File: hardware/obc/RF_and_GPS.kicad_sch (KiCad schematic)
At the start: 15 parts, among them J305 SMA RA Connector, J306 SMA RA Connector, J307 SMA RA Connector, U301 BMI088, U302 RFM98PW, U303 S1216V8, U304 GP2S1+

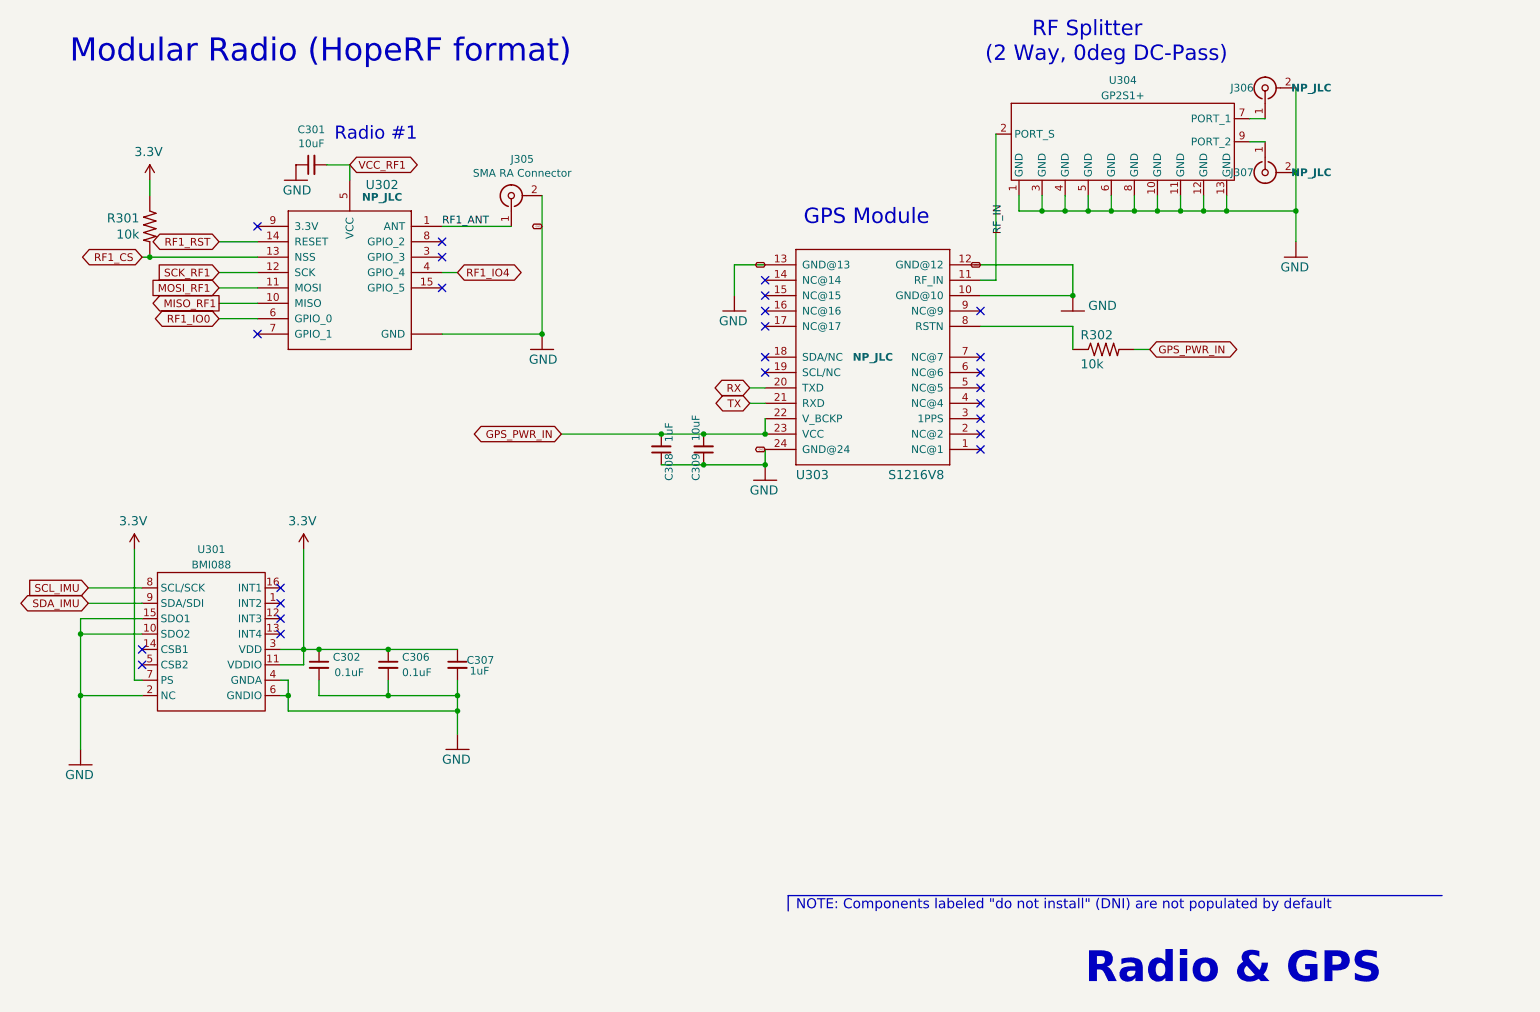
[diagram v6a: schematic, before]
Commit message: obc: Many schematic cleanups
Mostly alignment of components, adjustment of text.

Change SPI resistors to 27 ohms.
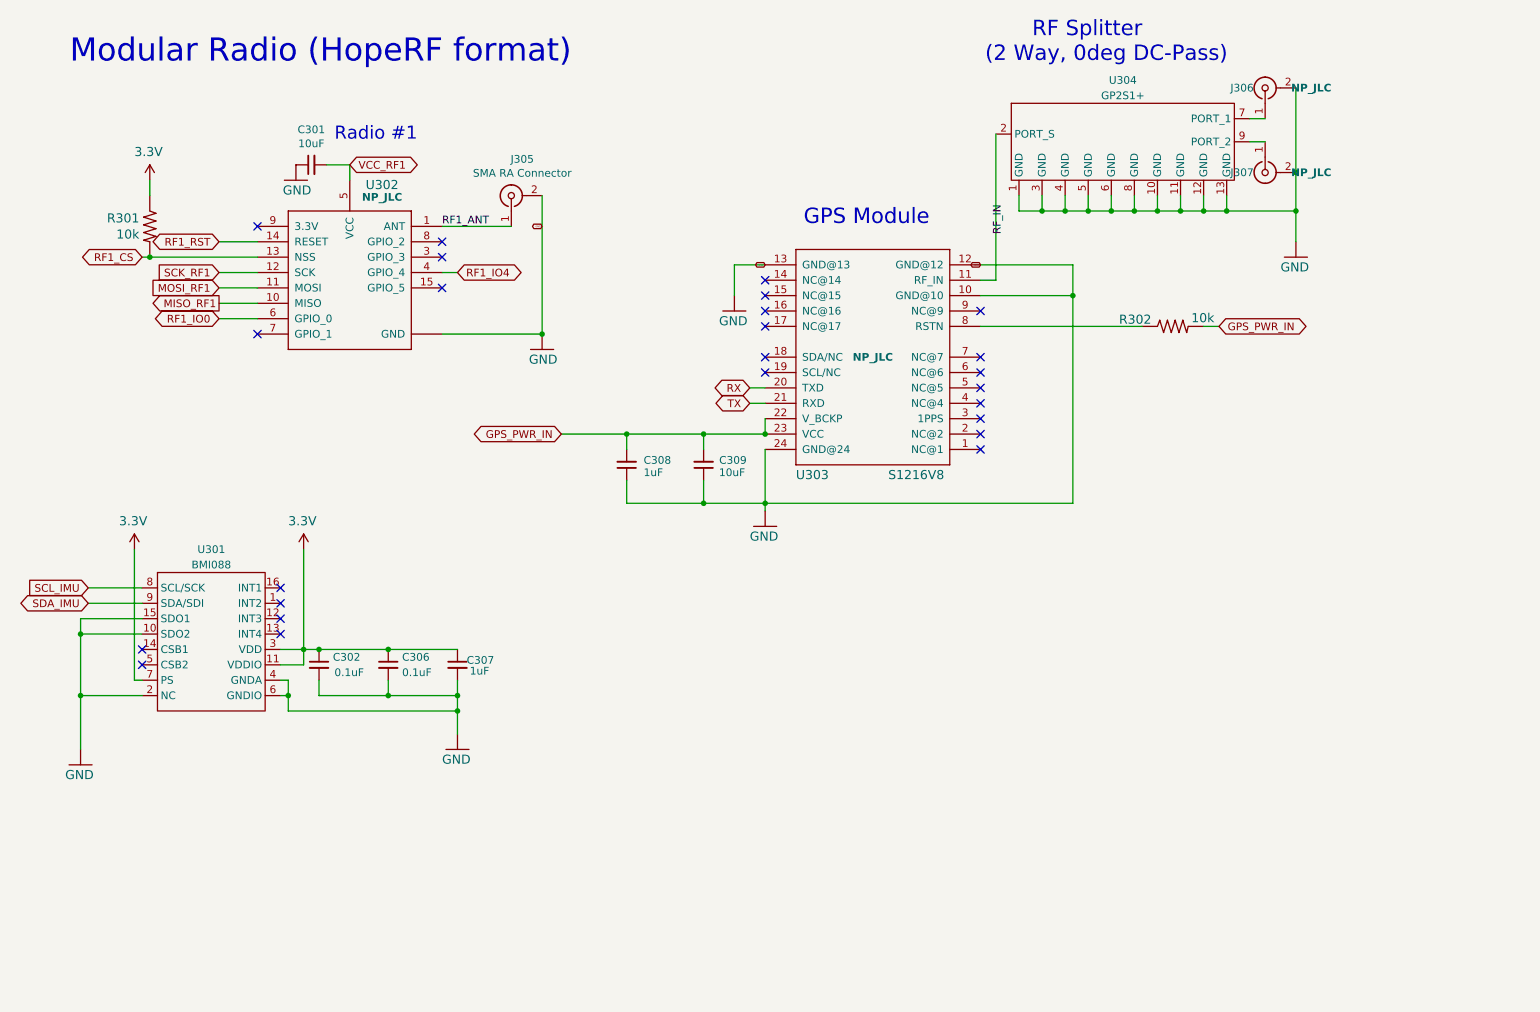
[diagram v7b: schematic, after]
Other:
- note removed: "NOTE: Components labeled "do not install" (DNI) are not populated by default"
- note removed: "Radio & GPS"
- moved on the sheet: C308, C309, R302

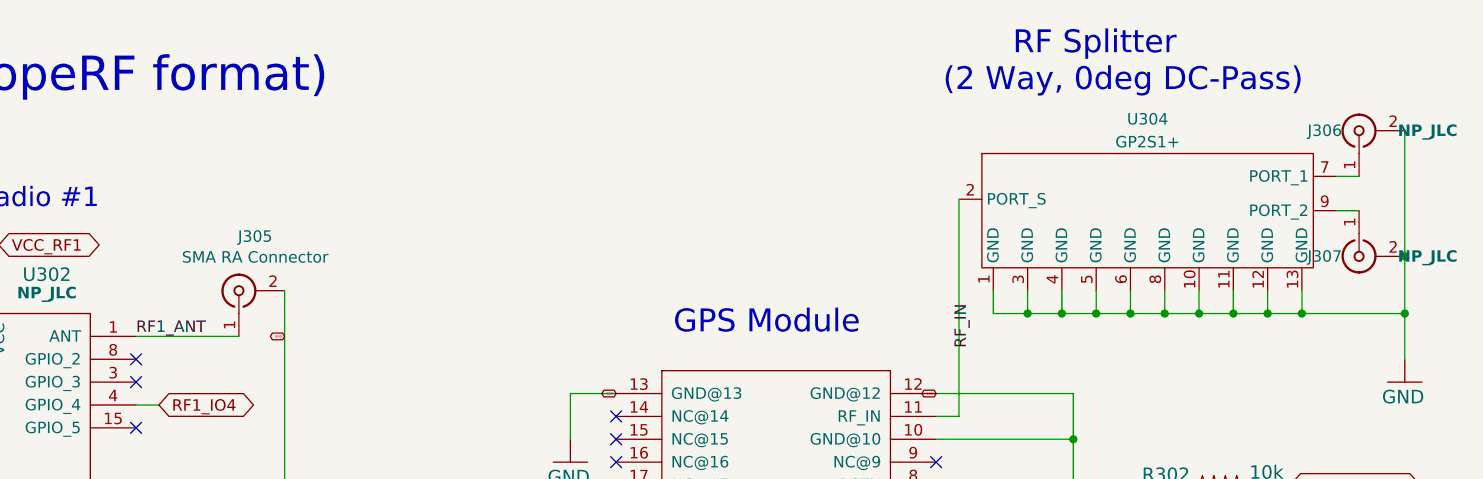
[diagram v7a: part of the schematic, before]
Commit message: obc: final (hopefully) design review for rev B
- Update some text
- Change some part values based on math (greater charge current)
- Increase design conservatism (place pullups on CS)

BOM review still needs to occur, including for a few parts that had
values changed in this pass (without part numbers being chosen)
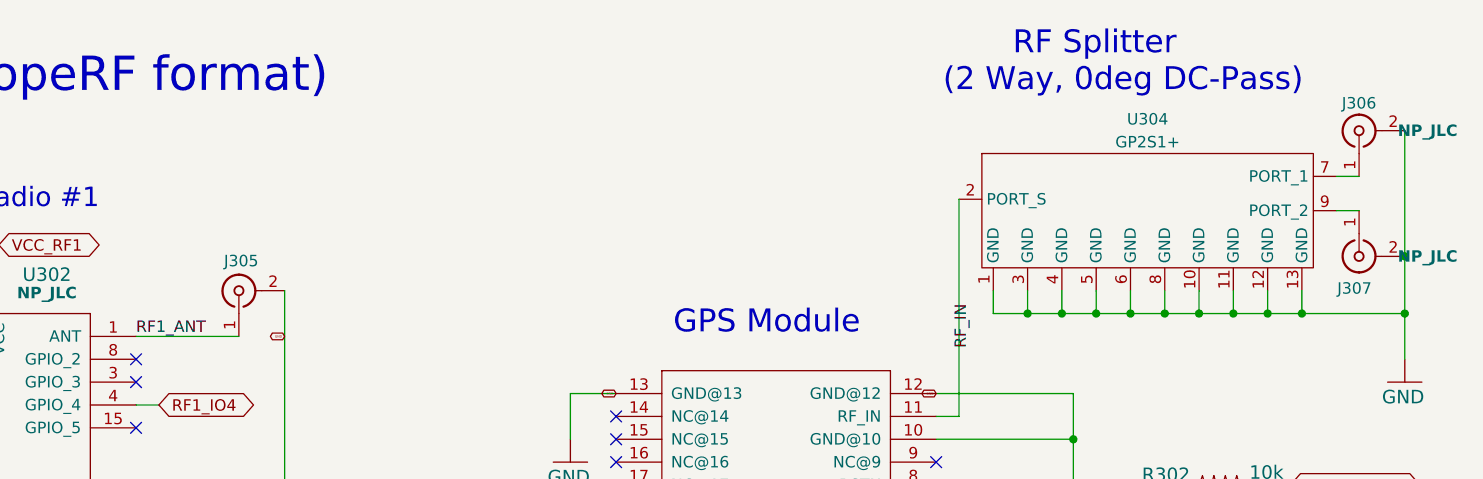
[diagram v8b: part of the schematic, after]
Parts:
- J305: value SMA RA Connector -> ~
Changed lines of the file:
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@@
 		(dnp no)
 		(property "Reference" "J306"
-			(at 233.68 35.56 90)
+			(at 237.49 32.512 90)
 			(effects
 				(font
@@
 		(dnp no)
 		(property "Reference" "J307"
-			(at 233.68 49.53 90)
+			(at 236.982 53.086 90)
 			(effects
 				(font
@@
 		(dnp no)
 		(property "Reference" "J305"
-			(at 114.8334 47.3202 90)
-			(effects
-				(font
-					(size 1.27 1.27)
-				)
-			)
-		)
-		(property "Value" "SMA RA Connector"
+			(at 113.284 50.038 90)
+			(effects
+				(font
+					(size 1.27 1.27)
+				)
+			)
+		)
+		(property "Value" "~"
 			(at 114.8334 49.6316 90)
 			(effects
